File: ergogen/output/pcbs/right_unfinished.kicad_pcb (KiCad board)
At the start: 2 copper layers, 140.9 x 102.2 mm, 49 parts

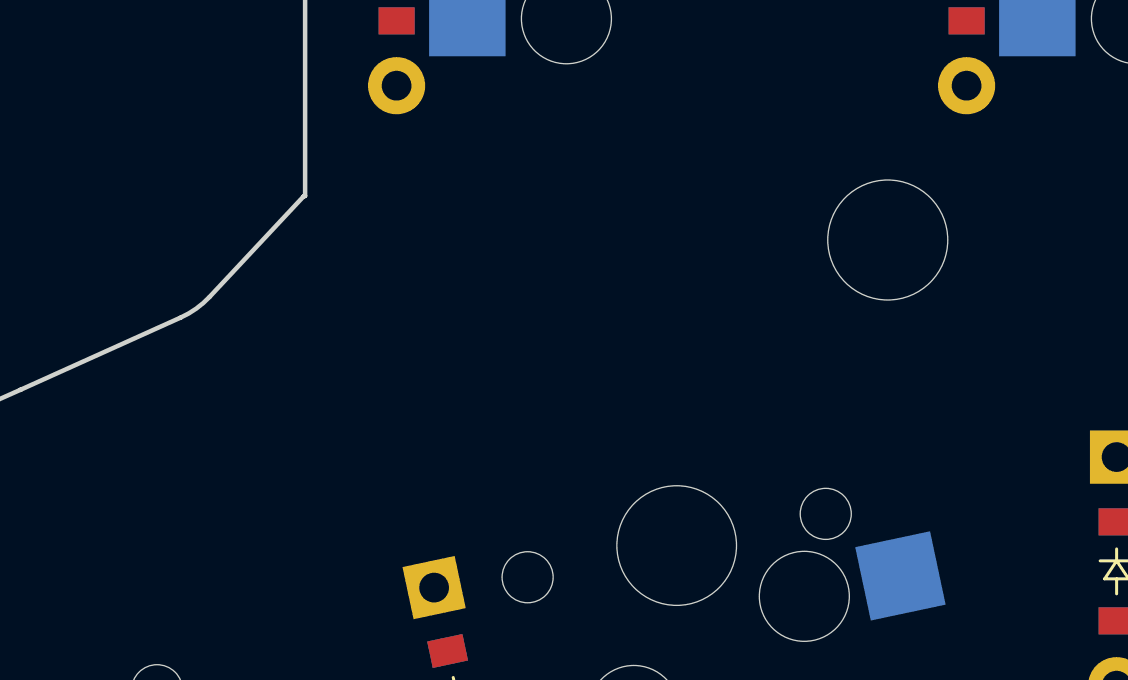
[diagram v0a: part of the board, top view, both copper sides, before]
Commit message: configured key nets correct
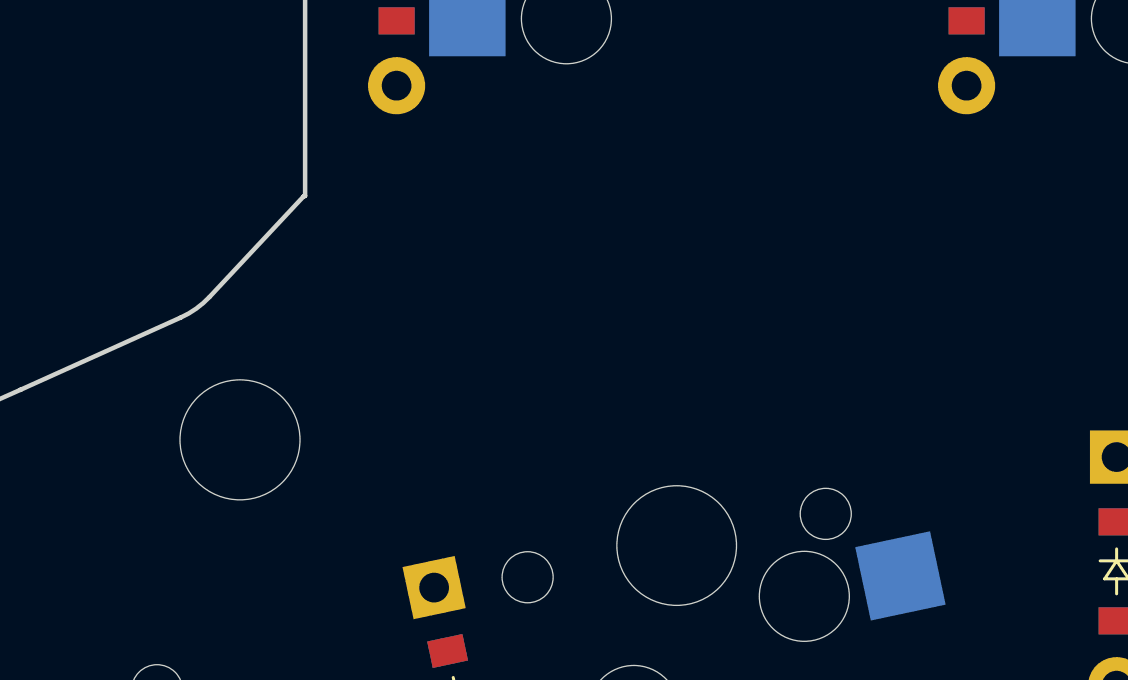
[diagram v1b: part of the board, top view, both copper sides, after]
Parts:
- moved ? 22.6 mm to (159.6, 16.1), turned to 24 degrees
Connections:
- D11 pad 1: P155 -> P115
- D12 pad 1: P155 -> P115
- D13 pad 1: P155 -> P115
- S18 pad 2: P155 -> P115
- S19 pad 2: P155 -> P115
- S20 pad 2: P155 -> P115

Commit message: Too many unrouted
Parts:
- removed the ? at (159.6, 16.1)
- removed the ? at (240.0, -10.5)
- removed the ? at (258.0, -29.5)
- removed the ? at (202.0, -42.5)
- removed the ? at (220.0, -21.5)
- added ?: , HOLE_M2_TH, F.Cu at (136.6, 124.1)
- added ?: , HOLE_M2_TH, F.Cu at (197.0, 86.5)
- added ?: , HOLE_M2_TH, F.Cu at (217.0, 97.5)
- added ?: , HOLE_M2_TH, F.Cu at (179.0, 65.5)
- added ?: , HOLE_M2_TH, F.Cu at (235.0, 78.5)
- moved D12 110.4 mm to (143.8, 132.8)
- moved S20 110.4 mm to (129.2, 134.5)
- moved B1 110.4 mm to (141.5, 94.5)
- moved D1 110.4 mm to (236.8, 92.5)
- moved D10 110.4 mm to (141.8, 108.5)
- moved D11 110.4 mm to (165.8, 128.5)
- moved D14 110.4 mm to (160.0, 68.5)
- moved D15 110.4 mm to (153.0, 94.5)
- moved D16 110.4 mm to (175.8, 76.5)
- moved D17 110.4 mm to (191.0, 65.5)
- moved D18 110.4 mm to (210.0, 88.5)
- moved D19 110.4 mm to (229.0, 97.5)
- moved D2 110.4 mm to (217.8, 111.5)
- moved D20 110.4 mm to (248.0, 78.5)
- moved D3 110.4 mm to (217.8, 73.5)
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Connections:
- S1 pad 1: P020 -> mirror_outer_home
- S10 pad 1: P100 -> mirror_middle_home
- S11 pad 1: P100 -> mirror_middle_top
- S12 pad 1: P011 -> mirror_index_bottom
- S13 pad 1: P011 -> mirror_index_home
- S14 pad 1: P011 -> mirror_index_top
- S15 pad 1: P017 -> mirror_inner_bottom
- S16 pad 1: P017 -> mirror_inner_home
- S17 pad 1: P017 -> mirror_inner_top
- S18 pad 1: P100 -> mirror_near_thumb
- S19 pad 1: P011 -> mirror_home_thumb
- S2 pad 1: P020 -> mirror_outer_top
- S20 pad 1: P017 -> mirror_far_thumb
- S3 pad 1: P022 -> mirror_pinky_bottom
- S4 pad 1: P022 -> mirror_pinky_home
- S5 pad 1: P022 -> mirror_pinky_top
- S6 pad 1: P024 -> mirror_ring_bottom
- S7 pad 1: P024 -> mirror_ring_home
- S8 pad 1: P024 -> mirror_ring_top
- S9 pad 1: P100 -> mirror_middle_bottom
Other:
- net class Default removed

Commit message: done with the pcbs finally
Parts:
- removed the ? at (136.6, 124.1)
- removed the ? at (197.0, 86.5)
- removed the ? at (217.0, 97.5)
- removed the ? at (179.0, 65.5)
- removed the ? at (235.0, 78.5)
- added ?: , HOLE_M2_TH, F.Cu at (159.6, 16.1)
- added ?: , HOLE_M2_TH, F.Cu at (240.0, -10.5)
- added ?: , HOLE_M2_TH, F.Cu at (258.0, -29.5)
- added ?: , HOLE_M2_TH, F.Cu at (202.0, -42.5)
- added ?: , HOLE_M2_TH, F.Cu at (220.0, -21.5)
- moved D12 110.4 mm to (166.8, 24.8), turned to -258 degrees
- moved S20 110.4 mm to (152.2, 26.5)
- moved B1 110.4 mm to (164.5, -13.5)
- moved D1 110.4 mm to (259.8, -15.5), turned to -270 degrees
- moved D10 110.4 mm to (164.8, 0.50), turned to -270 degrees
- moved D11 110.4 mm to (188.8, 20.5), turned to -270 degrees
- moved D14 110.4 mm to (183.0, -39.5), turned to -270 degrees
- moved D15 110.4 mm to (176.0, -13.5)
- moved D16 110.4 mm to (198.8, -31.5), turned to -270 degrees
- moved D17 110.4 mm to (214.0, -42.5)
- moved D18 110.4 mm to (233.0, -19.5)
- moved D19 110.4 mm to (252.0, -10.5)
- moved D2 110.4 mm to (240.8, 3.50), turned to -270 degrees
- moved D20 110.4 mm to (271.0, -29.5)
- moved D3 110.4 mm to (240.8, -34.5), turned to -270 degrees
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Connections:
- S1 pad 1: mirror_outer_home -> P020
- S1 pad 2: P029 -> mirror_outer_home
- S10 pad 1: mirror_middle_home -> P100
- S10 pad 2: P029 -> mirror_middle_home
- S11 pad 1: mirror_middle_top -> P100
- S11 pad 2: P031 -> mirror_middle_top
- S12 pad 1: mirror_index_bottom -> P011
- S12 pad 2: P002 -> mirror_index_bottom
- S13 pad 1: mirror_index_home -> P011
- S13 pad 2: P029 -> mirror_index_home
- S14 pad 1: mirror_index_top -> P011
- S14 pad 2: P031 -> mirror_index_top
- S15 pad 1: mirror_inner_bottom -> P017
- S15 pad 2: P002 -> mirror_inner_bottom
- S16 pad 1: mirror_inner_home -> P017
- S16 pad 2: P029 -> mirror_inner_home
- S17 pad 1: mirror_inner_top -> P017
- S17 pad 2: P031 -> mirror_inner_top
- S18 pad 1: mirror_near_thumb -> P100
- S18 pad 2: P115 -> mirror_near_thumb
- S19 pad 1: mirror_home_thumb -> P011
- S19 pad 2: P115 -> mirror_home_thumb
- S2 pad 1: mirror_outer_top -> P020
- S2 pad 2: P031 -> mirror_outer_top
- S20 pad 1: mirror_far_thumb -> P017
- S20 pad 2: P115 -> mirror_far_thumb
- S3 pad 1: mirror_pinky_bottom -> P022
- S3 pad 2: P002 -> mirror_pinky_bottom
- S4 pad 1: mirror_pinky_home -> P022
- S4 pad 2: P029 -> mirror_pinky_home
- S5 pad 1: mirror_pinky_top -> P022
- S5 pad 2: P031 -> mirror_pinky_top
- S6 pad 1: mirror_ring_bottom -> P024
- S6 pad 2: P002 -> mirror_ring_bottom
- S7 pad 1: mirror_ring_home -> P024
- S7 pad 2: P029 -> mirror_ring_home
- S8 pad 1: mirror_ring_top -> P024
- S8 pad 2: P031 -> mirror_ring_top
- S9 pad 1: mirror_middle_bottom -> P100
- S9 pad 2: P002 -> mirror_middle_bottom
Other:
- net class Default added: clearance 0.2, trace_width 0.25, via_dia 0.8, via_drill 0.4
